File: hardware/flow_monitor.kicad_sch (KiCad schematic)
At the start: 77 parts, among them J1 Conn_01x04_Pin, J2 USB_C_Receptacle_USB2.0_16P, J3 Conn_01x02_Socket, J4 Conn_01x02_Socket, J5 Conn_01x02_SocketTOP, J6 Conn_01x02_Socket, J7 Conn_01x02_SocketBOT, Q1 2N7002, Q2 IRLML6402, Q3 BC807, Q4 BC817, Q5 2N7002, Q6 2N7002, SW2 1TS005F-2500-5001, SW4 1TS005F-2500-5001, SW5 SW_SPDT, U1 USBLC6-2SC6, U2 BQ25185DLHR, U3 CH340C, U4 TPS631000, U6 STM32G030C8Tx, U7 EA_DOGS164W-A, Y1 Crystal

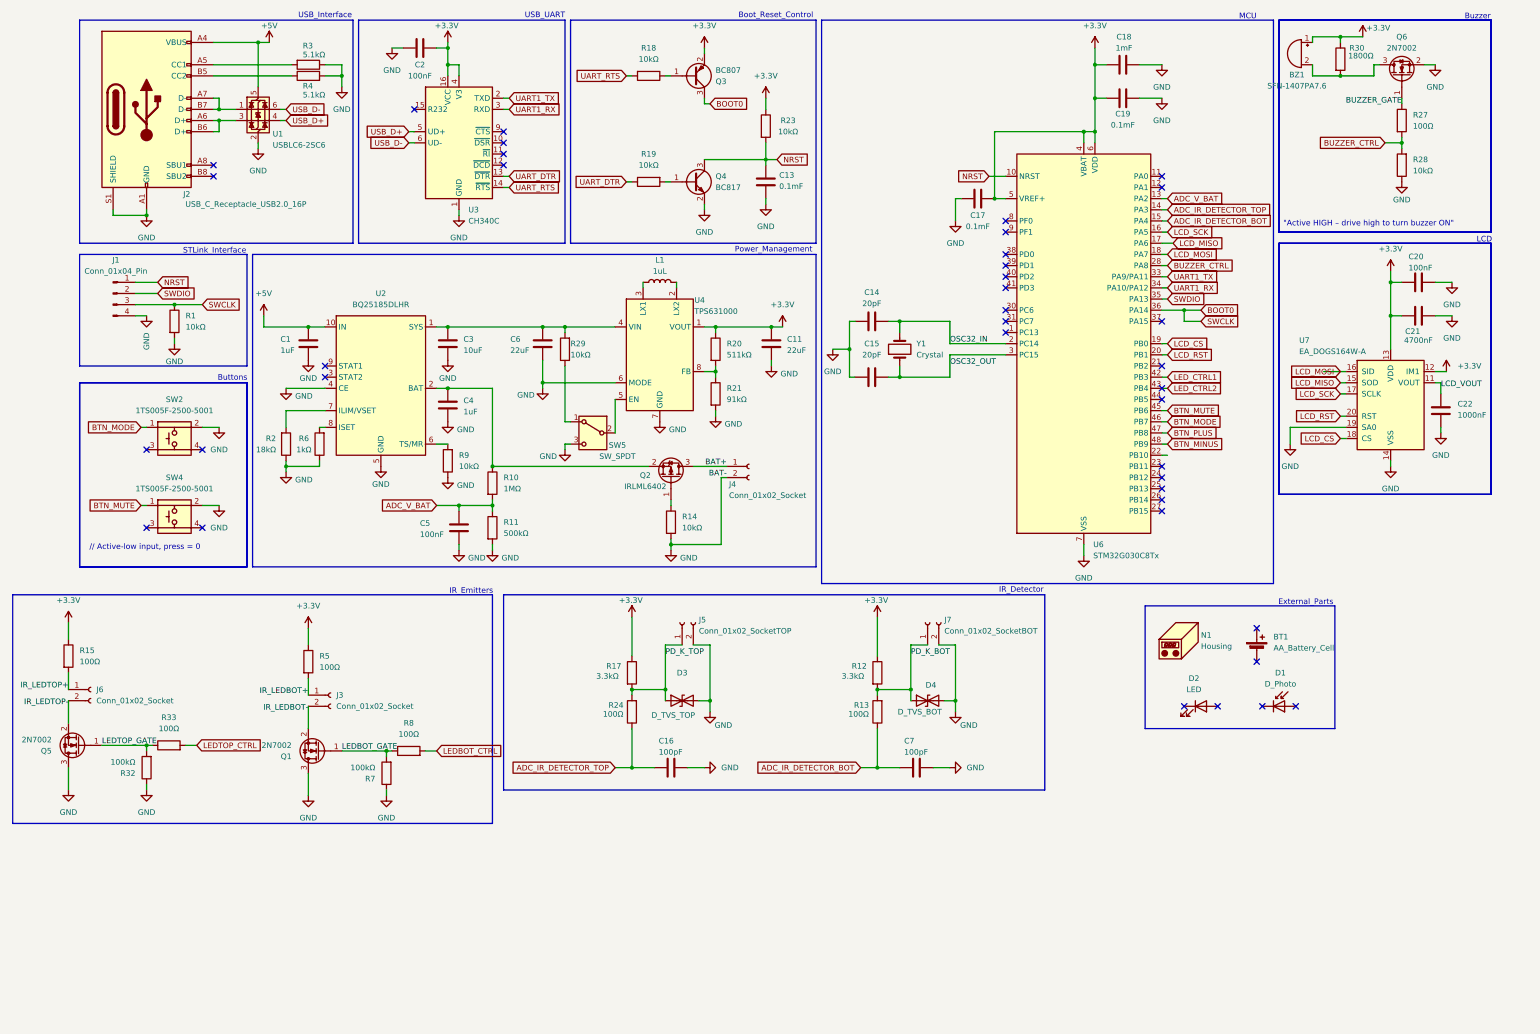
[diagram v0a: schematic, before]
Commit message: hardware: snapshot before power architecture change
Commit current schematic, PCB, and firmware state as a clean
restore point prior to reworking the power supply architecture.
Also adds KiCad autosave/backup patterns to .gitignore.

Co-Authored-By: Claude Sonnet 4.6 <noreply@anthropic.com>
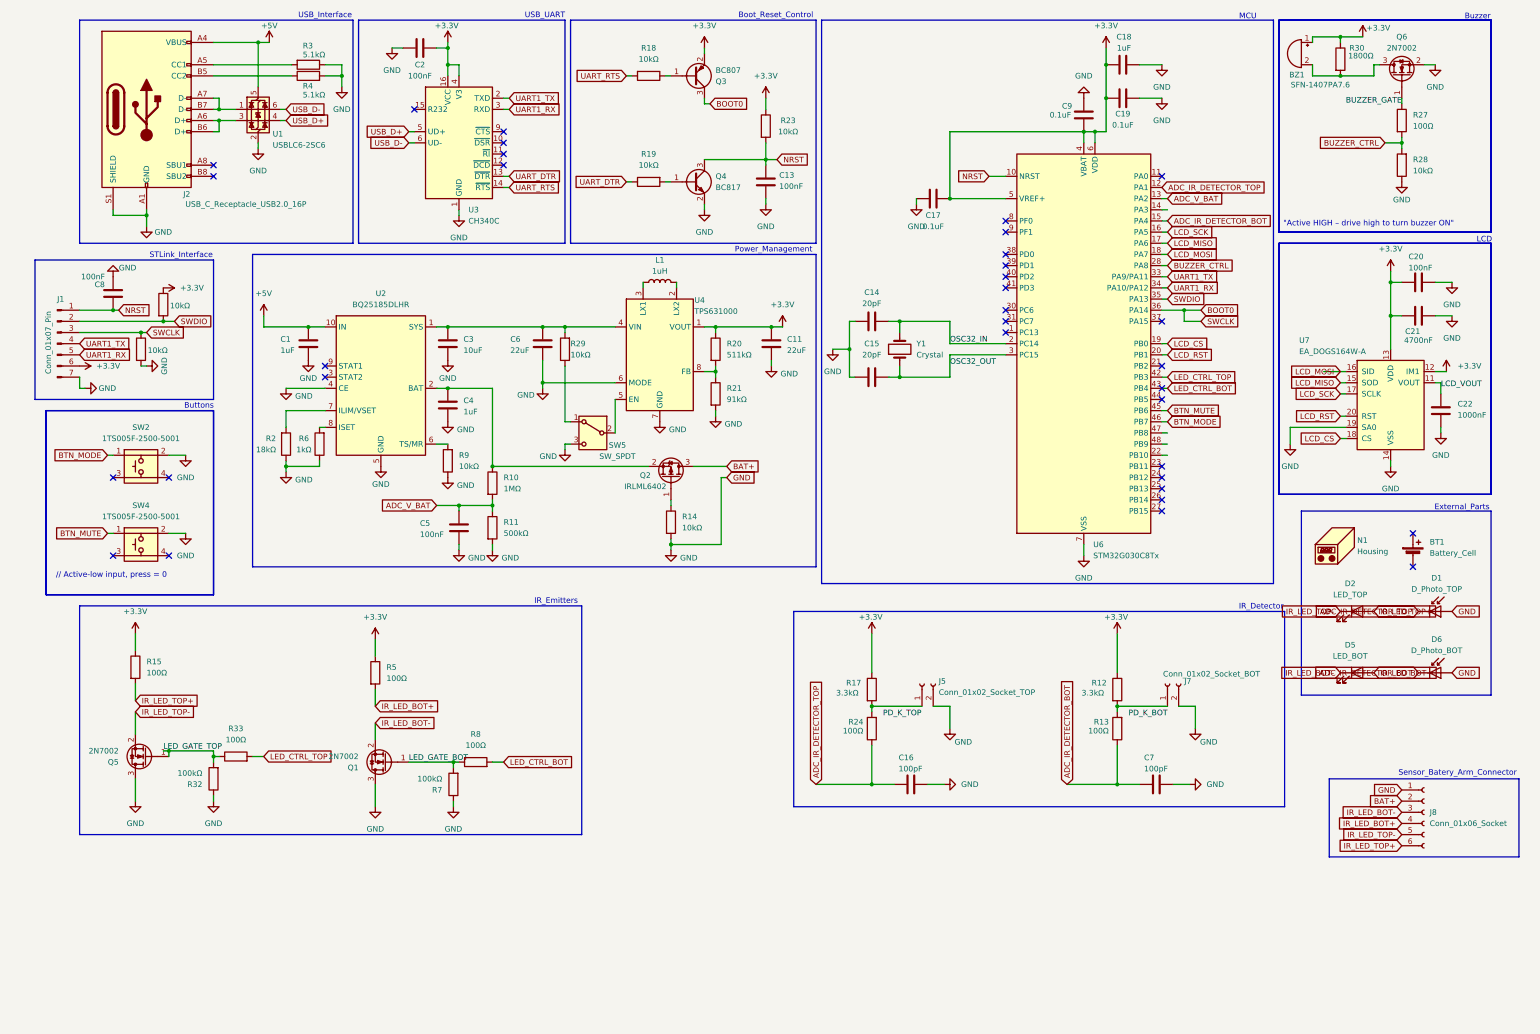
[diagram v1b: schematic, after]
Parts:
- removed D3: D_TVS_TOP, symbol Device:D_TVS
- removed D4: D_TVS_BOT, symbol Device:D_TVS
- removed J1: Conn_01x04_Pin, Connector_PinHeader_2.54mm:PinHeader_1x04_P2.54mm_Vertical, symbol Connector:Conn_01x04_Pin
- removed J3, J6: Conn_01x02_Socket, Connector_Wire:SolderWire-0.1sqmm_1x02_P3.6mm_D0.4mm_OD1mm_Relief, symbol Connector:Conn_01x02_Socket
- removed J4: Conn_01x02_Socket, Connector_Molex:Molex_PicoBlade_53048-0210_1x02_P1.25mm_Horizontal, symbol Connector:Conn_01x02_Socket
- added C8: 100nF, Capacitor_SMD:C_0603_1608Metric, symbol Device:C
- added C9: 0.1uF, Capacitor_SMD:C_0603_1608Metric, symbol Device:C
- added D5: LED_BOT, symbol Device:LED
- added D6: D_Photo_BOT, symbol Device:D_Photo
- added J1: Conn_01x07_Pin, Connector_PinHeader_2.54mm:PinHeader_1x07_P2.54mm_Vertical, symbol Connector:Conn_01x07_Pin
- added J8: Conn_01x06_Socket, Connector_FFC-FPC:Jushuo_AFC07-S06FCA-00_1x6-1MP_P0.50_Horizontal, symbol Connector:Conn_01x06_Socket
- added R16: 10kΩ, Resistor_SMD:R_0603_1608Metric, symbol Device:R
- BT1: value AA_Battery_Cell -> Battery_Cell
- C13: value 0.1mF -> 100nF
- C17, C19: value 0.1mF -> 0.1uF
- C18: value 1mF -> 1uF
- D1: value D_Photo -> D_Photo_TOP
- D2: value LED -> LED_TOP
- J5: value Conn_01x02_SocketTOP -> Conn_01x02_Socket_TOP
- J7: value Conn_01x02_SocketBOT -> Conn_01x02_Socket_BOT
- L1: value 1uL -> 1uH
- R30: footprint (none) -> Resistor_SMD:R_0603_1608Metric
- SW5: footprint IV_Flow_Monitor_Footprints:UNFINIDHED_SW_Slide_SPDT_SSK12D07VG5 -> IV_Flow_Monitor_Footprints:X_SW_Slide_SPDT_SSK12D07VG5
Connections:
- net IR_LEDTOP+ is gone; now on net IR_LED_TOP+: R15.2
- net IR_LEDTOP- is gone; now on net IR_LED_TOP-: Q5.2 (S)
- net LED_CTRL1 is gone; now on net LED_CTRL_TOP: U6.42 (PB3)
- net LED_CTRL2 is gone; now on net LED_CTRL_BOT: U6.43 (PB4)
- net +3.3V: now also C9.1, J1.6 (Pin_6), R16.1
- net ADC_IR_DETECTOR_BOT: now also D6.1 (K)
- net ADC_IR_DETECTOR_TOP: now also D1.1 (K), U6.12 (PA1); no longer U6.14 (PA3)
- net BAT+: now also J8.2 (Pin_2)
- net BOOT0: now also J1.3 (Pin_3)
- net GND: now also D1.2 (A), C8.2, C9.2, D6.2 (A), J1.7 (Pin_7), J8.1 (Pin_1)
- net NRST: now also C8.1, J1.1 (Pin_1)
- net PD_K_BOT: no longer J7.1 (Pin_1), R12.2, R13.2
- net PD_K_TOP: no longer J5.1 (Pin_1), R17.2, R24.2
- net SWDIO: now also J1.2 (Pin_2), R16.2
- net UART1_RX: now also J1.5 (Pin_5)
- net UART1_TX: now also J1.4 (Pin_4)
- net IR_LED_TOP-: now reaches D2.1 (K)
- net IR_LED_TOP-: now also J8.5 (Pin_5)
- net IR_LED_TOP+: now reaches D2.2 (A)
- net IR_LED_TOP+: now also J8.6 (Pin_6)
- net BTN_MINUS: no longer names the net of U6.48 (PB9)
- net BTN_PLUS: no longer names the net of U6.47 (PB8)
- net IR_LEDBOT+ renamed IR_LED_BOT+
- net IR_LED_BOT+: now also D5.2 (A), J8.4 (Pin_4)
- net IR_LEDBOT- renamed IR_LED_BOT-
- net IR_LED_BOT-: now also D5.1 (K), J8.3 (Pin_3)
- net LEDBOT_CTRL renamed LED_CTRL_BOT
- net LEDBOT_GATE renamed LED_GATE_BOT
- net LEDTOP_CTRL renamed LED_CTRL_TOP
- net LEDTOP_GATE renamed LED_GATE_TOP
- new net: J7.1 (Pin_1), R12.2, R13.2
- new net: J5.1 (Pin_1), R17.2, R24.2
- no-connect marks 39 -> 34
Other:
- note added: "Sensor_Batery_Arm_Connector"
- moved on the sheet: BT1, C16, C17, C7, D1, D2, J5, J7, N1, Q1, Q5, R12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

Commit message: power: add TPS610982DSET boost converter circuit (components placed, wiring needs KiCad fixup)
All 13 new power supply components placed with correct values and MPNs:
U4 TPS610982DSET, L2 4.7uH, C1 10uF, C2 100nF, C3 22uF, C4 100nF,
R2 33R (input filter), R3/R4/R6 100k (MODE network), R9 100k (gate),
Q3 AO3401A (reverse polarity), SW5 SK12D07VG5 (power switch).
New lib_symbols added: Device:L, Transistor_FET:AO3401A, Switch:SW_SPDT,
IV_Flow_Monitor_Symbols:TPS610982DSET.
Wire endpoints need alignment in KiCad GUI — see wiring fixup notes.

Co-Authored-By: Claude Sonnet 4.6 <noreply@anthropic.com>
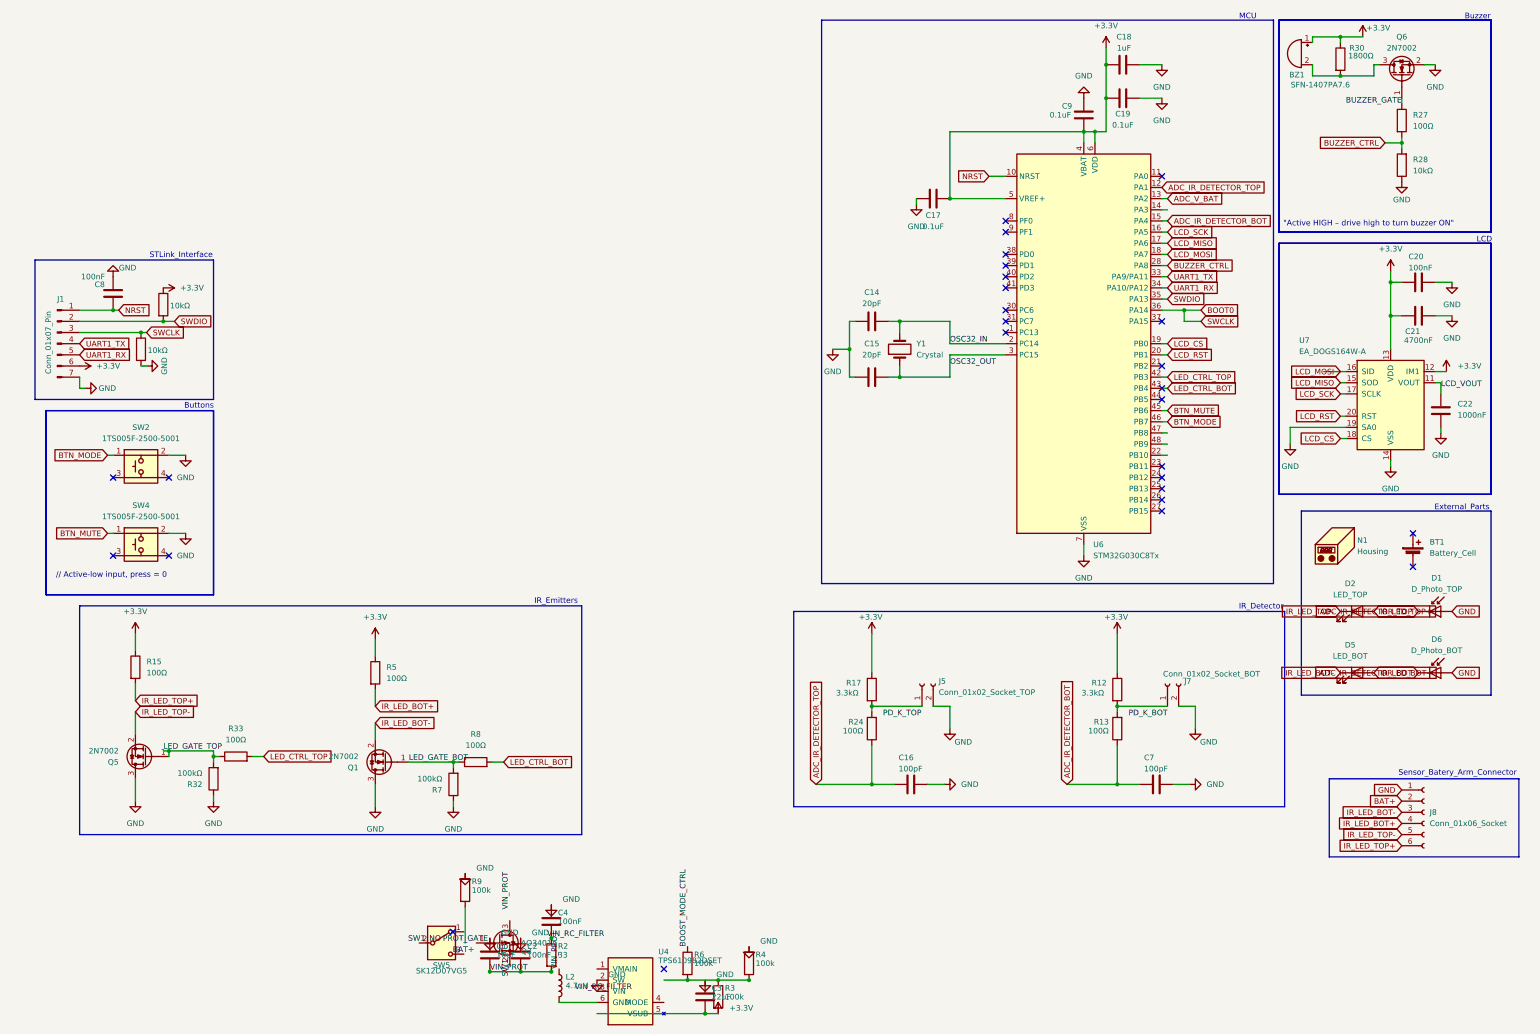
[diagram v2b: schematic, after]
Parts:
- removed C11, C6: 22uF, Capacitor_SMD:C_0603_1608Metric, symbol Device:C
- removed C13, C5: 100nF, Capacitor_SMD:C_0603_1608Metric, symbol Device:C
- removed J2: USB_C_Receptacle_USB2.0_16P, IV_Flow_Monitor_Footprints:USB_C_Receptacle_GCT_USB4105-xx-A_16P_TopMnt_Horizontal, symbol Connector:USB_C_Receptacle_USB2.0_16P
- removed L1: 1uH, Inductor_SMD:L_0805_2012Metric, symbol Device:L
- removed Q2: IRLML6402, Package_TO_SOT_SMD:SOT-23, symbol Transistor_FET:IRLML6402
- removed Q3: BC807, Package_TO_SOT_SMD:SOT-23, symbol Transistor_BJT:BC807
- removed Q4: BC817, Package_TO_SOT_SMD:SOT-23, symbol Transistor_BJT:BC817
- removed R10: 1MΩ, Resistor_SMD:R_0603_1608Metric, symbol Device:R
- removed R11: 500kΩ, Resistor_SMD:R_0603_1608Metric, symbol Device:R
- removed R14, R18, R19, R23, R29: 10kΩ, Resistor_SMD:R_0603_1608Metric, symbol Device:R
- removed R20: 511kΩ, Resistor_SMD:R_0603_1608Metric, symbol Device:R
- removed R21: 91kΩ, Resistor_SMD:R_0603_1608Metric, symbol Device:R
- removed U1: USBLC6-2SC6, Package_TO_SOT_SMD:SOT-23-6, symbol Power_Protection:USBLC6-2SC6
- removed U2: BQ25185DLHR, Package_SON:WSON-10-1EP_2x3mm_P0.5mm_EP0.84x2.4mm_ThermalVias, symbol IV_Flow_Monitor_Symbols:BQ25185DLHR
- removed U3: CH340C, Package_SO:SOIC-16_3.9x9.9mm_P1.27mm, symbol Interface_USB:CH340C
- removed U4: TPS631000, Package_TO_SOT_SMD:SOT-583-8, symbol IV_Flow_Monitor_Symbols:TPS631000
- added L2: 4.7uH, Inductor_SMD:L_0806_2016Metric, symbol Device:L
- added Q3: AO3401A, Package_TO_SOT_SMD:SOT-23, symbol Transistor_FET:AO3401A
- added U4: TPS610982DSET, Package_SON:Texas_DSE-6, symbol IV_Flow_Monitor_Symbols:TPS610982DSET
- C1: value 1uF -> 10uF; MPN (none) -> GRM188R60J106ME47D; Mfr. No. CL10B105KA8NNND -> (none)
- C2: MPN (none) -> GCM188R71H104KA57J
- C3: value 10uF -> 22uF; footprint Capacitor_SMD:C_1206_3216Metric -> Capacitor_SMD:C_0603_1608Metric; MPN (none) -> GRM21BR60J226ME39L; Mfr. No. CL31B106KAHNNNE -> (none)
- C4: value 1uF -> 100nF; MPN (none) -> CL10B104KA8NNNC; Mfr. No. CL10B105KA8NNND -> (none)
- R2: value 18kΩ -> 33; MPN (none) -> RC0603JR-07330RL
- R3, R4: value 5.1kΩ -> 100k; MPN (none) -> RC0603FR-07100KL
- R6: value 1kΩ -> 100k; MPN (none) -> RC0603FR-07100KL
- R9: value 10kΩ -> 100k; MPN (none) -> RC0603FR-07100KL
- SW5: value SW_SPDT -> SK12D07VG5; footprint IV_Flow_Monitor_Footprints:X_SW_Slide_SPDT_SSK12D07VG5 -> (none); MPN (none) -> SK12D07VG5
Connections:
- net +5V is gone; now on net VIN_PROT: C1.2
- net +3.3V: now also C3.2, R3.2; no longer C2.1
- net GND: now also C2.1, R4.1, U4.2 (SW); no longer C2.2, R2.1, R3.1, R4.2, R6.1, SW5.3 (C)
- net at R6.2: now also R3.1, R4.2
- net at C4.2: now also R2.1
- net VIN_PROT: now reaches R2.2
- net VIN_PROT: now also C2.2, L2.1
- new net: L2.2, U4.6 (GND)
- new net BOOST_MODE_CTRL: R6.1
- no-connect marks 34 -> 27
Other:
- note removed: "Boot_Reset_Control"
- note removed: "Power_Management"
- note removed: "USB_Interface"
- note removed: "USB_UART"
